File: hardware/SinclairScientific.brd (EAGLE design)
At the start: 50.8 x 22.9 mm, 33 parts, among them SW1 SPST_TACT-KMR2, U2 SPX3819-3.3, U3 MCP73831T-2ACI/OT, X1 JSTPH, X2 32.768, X3 microUSB

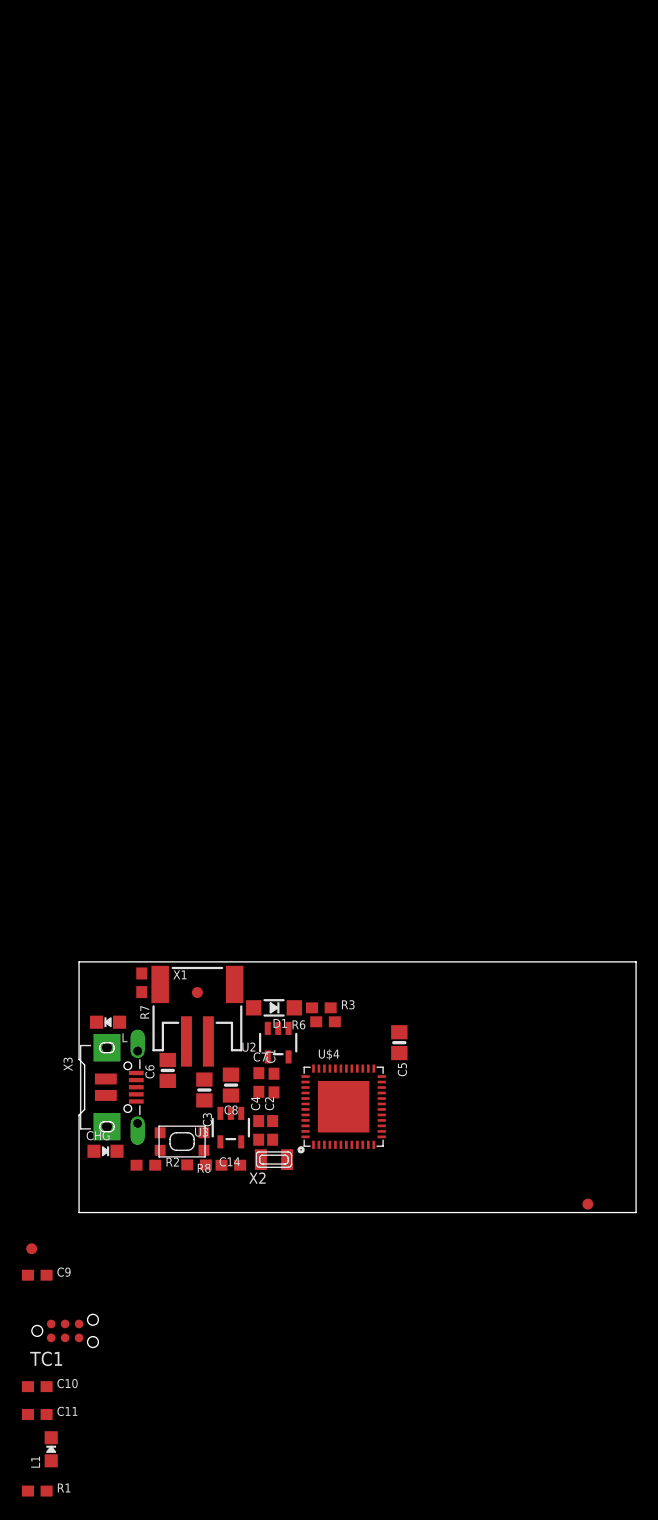
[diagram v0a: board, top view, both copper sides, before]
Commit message: Added more to schematic, started PCB placement, still WIP
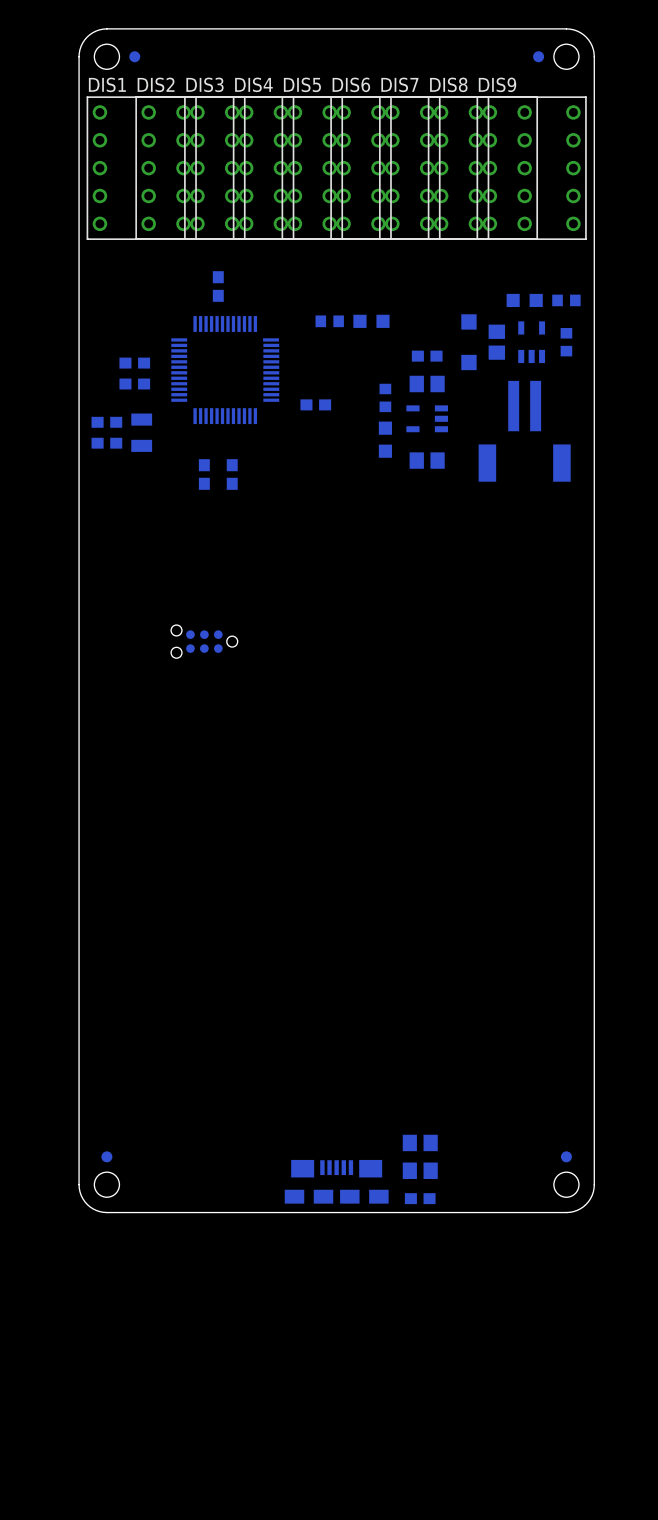
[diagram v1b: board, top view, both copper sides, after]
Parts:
- removed L: RED, SinclairScientific:CHIPLED_0805_NOOUTLINE
- removed R3: 100k, SinclairScientific:0603-NO
- removed R6: 100K, SinclairScientific:0603-NO
- removed SW1: SPST_TACT-KMR2, SinclairScientific:KMR2
- removed U$4: ATSAMD21G18_QFN, SinclairScientific:TQFN48_7MM
- removed X1: JSTPH, SinclairScientific:JSTPH2
- removed X3: microUSB, SinclairScientific:4UCONN_20329_V2
- added C12: 1uF, gametroller:C0603
- added C13: 10uF, gametroller:C0805
- added DIS1, DIS2, DIS3, DIS4, DIS5, DIS6, DIS7, DIS8, DIS9: LED_7-SEGMENT, SinclairScientific:HDSP-E
- added F1: 500mA, gametroller:R0805
- added J1: JSTPH, SinclairScientific:JSTPH2
- added J3: USB-MICRO, gametroller:USB-10118192-0001LF
- added L2: RED, SinclairScientific:CHIPLED_0805_NOOUTLINE
- added U$2: FIDUCIAL"", SinclairScientific:FIDUCIAL_1MM
- added U4: ATSAMD21G18, gametroller:TQFP48_7MM
- C1, C10, C11, C14, C2, C4, C7, C9: device SinclairScientific:0603-NO -> gametroller:C0603
- C3, C6, C8: value 10µF -> 10uF; device SinclairScientific:0805-NO -> gametroller:C0805
- C5: value 10uF -> 100nF; device SinclairScientific:0805-NO -> gametroller:C0603
- R1, R2, R7, R8: device SinclairScientific:0603-NO -> gametroller:R0603
- moved R1 104.6 mm to (27.9, 74.3), flipped to the bottom, turned to 270 degrees
- moved C10 101.7 mm to (12.7, 84.5), flipped to the bottom, turned to 90 degrees
- moved L1 97.0 mm to (27.9, 70.5), flipped to the bottom, turned to 180 degrees
- moved C11 95.5 mm to (21.6, 73.7), flipped to the bottom, turned to 180 degrees
- moved R2 87.7 mm to (44.5, 83.2), flipped to the bottom, turned to 180 degrees
- moved CHG 86.5 mm to (40.6, 83.2), flipped to the bottom, turned to 90 degrees
- moved U$34 85.5 mm to (5.08, 105.4), flipped to the bottom
- moved C9 83.7 mm to (5.08, 77.5), flipped to the bottom
- moved R8 81.1 mm to (44.5, 79.4), flipped to the bottom, turned to 270 degrees
- moved U3 76.7 mm to (41.3, 79.4), flipped to the bottom, turned to 0 degrees
- moved C3 73.2 mm to (38.1, 79.4), flipped to the bottom, turned to 90 degrees
- moved C14 71.4 mm to (5.08, 75.6), flipped to the bottom
- moved C7 68.0 mm to (31.8, 78.1), flipped to the bottom, turned to 180 degrees
- moved X2 67.4 mm to (5.71, 71.1), flipped to the bottom, turned to 270 degrees
- moved C8 66.4 mm to (31.8, 75.6), flipped to the bottom, turned to 180 degrees
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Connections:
- removed net D+: U$4.34, X3.D+
- removed net D-: U$4.33, X3.D-
- removed net GND1: L1.C
- new net LED_A: DIS1.10, DIS2.10, DIS3.10, DIS4.10, DIS5.10, DIS6.10, DIS7.10, DIS8.10, DIS9.10
- new net LED_B: DIS1.9, DIS2.9, DIS3.9, DIS4.9, DIS5.9, DIS6.9, DIS7.9, DIS8.9, DIS9.9
- new net LED_C: DIS1.7, DIS2.7, DIS3.7, DIS4.7, DIS5.7, DIS6.7, DIS7.7, DIS8.7, DIS9.7
- new net LED_CA1: DIS1.3, DIS1.8
- new net LED_CA2: DIS2.3, DIS2.8
- new net LED_CA3: DIS3.3, DIS3.8
- new net LED_CA4: DIS4.3, DIS4.8
- new net LED_CA5: DIS5.3, DIS5.8
- new net LED_CA6: DIS6.3, DIS6.8
- new net LED_CA7: DIS7.3, DIS7.8
- new net LED_CA8: DIS8.3, DIS8.8
- new net LED_CA9: DIS9.3, DIS9.8
- new net LED_D: DIS1.5, DIS2.5, DIS3.5, DIS4.5, DIS5.5, DIS6.5, DIS7.5, DIS8.5, DIS9.5
- new net LED_DP: DIS1.6, DIS2.6, DIS3.6, DIS4.6, DIS5.6, DIS6.6, DIS7.6, DIS8.6, DIS9.6
- new net LED_E: DIS1.4, DIS2.4, DIS3.4, DIS4.4, DIS5.4, DIS6.4, DIS7.4, DIS8.4, DIS9.4
- new net LED_F: DIS1.2, DIS2.2, DIS3.2, DIS4.2, DIS5.2, DIS6.2, DIS7.2, DIS8.2, DIS9.2
- new net LED_G: DIS1.1, DIS2.1, DIS3.1, DIS4.1, DIS5.1, DIS6.1, DIS7.1, DIS8.1, DIS9.1
- new net N$8: F1.1, J3.1
- new net RXD: U4.38
- new net RXLED: U4.48
- new net TXD: U4.37
- new net TXLED: U4.39
- new net USB_DM: J3.2, U4.33
- new net USB_DP: J3.3, U4.34
- net !RESET: now also TC1.1, U4.40; no longer SW1.1, SW1.3, U$4.40
- net +3V3: now also R1.1, TC1.2, U4.17, U4.36, U4.44, U4.6; no longer U$4.17, U$4.36, U$4.44, U$4.6
- net A0: now also U4.3; no longer U$4.3
- net A1: now also U4.7; no longer U$4.7
- net A2: now also U4.8; no longer U$4.8
- net A3: now also U4.9; no longer U$4.9
- net A4: now also U4.10; no longer U$4.10
- net A5: now also U4.47; no longer U$4.47
- net AREF: now also U4.4; no longer U$4.4
- net D0: now also U4.16; no longer U$4.16
- net D1: now also U4.15; no longer U$4.15
- net D10: now also U4.27; no longer U$4.27
- net D11: now also U4.25; no longer U$4.25
- net D12: now also U4.28; no longer U$4.28
- net D13: now also U4.26; no longer U$4.26
- net D2: now also U4.23; no longer U$4.23
- net D3: now also U4.14; no longer U$4.14
- net D4: now also U4.13; no longer U$4.13
- net D5: now also U4.24; no longer U$4.24
- net D6: now also U4.29; no longer U$4.29
- net D7: now also U4.30; no longer U$4.30
- net D8: now also U4.11; no longer U$4.11
- net D9: now also U4.12; no longer R3.2, R6.1, U$4.12
- net GND: now also C12.2, C13.2, J1.1, J3.5, L1.C, L2.C, TC1.3, U4.18, U4.35, U4.42, U4.5; no longer L.C, R6.2, SW1.2, SW1.4, U$4.18, U$4.35, U$4.42, U$4.5, U$4.THERMAL, X1.1, X3.BASE@1, X3.BASE@2, X3.GND, X3.SPRT@1, X3.SPRT@2, X3.SPRT@3, X3.SPRT@4
- net MISO: now also U4.21; no longer U$4.21
- net MOSI: now also U4.19; no longer U$4.19
- net N$2: now also L2.A; no longer L.A
- net N$5: now also U4.1; no longer U$4.1
- net N$7: now also U4.2; no longer U$4.2
- net SCK: now also U4.20; no longer U$4.20
- net SCL: now also U4.32; no longer U$4.32
- net SDA: now also U4.31; no longer U$4.31
- net SWCLK: now also TC1.5, U4.45; no longer U$4.45
- net SWDIO: now also TC1.4, U4.46; no longer U$4.46
- net VBAT: now also J1.2; no longer R3.1, X1.2
- net VBUS: now also C12.1, C13.1, F1.2; no longer X3.VBUS
- net VDDCORE: now also U4.43; no longer U$4.43
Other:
- board size 50.8 x 22.9 mm -> 47 x 108 mm

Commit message: Schematic nearly finalized, still working on board dimensions and component placement
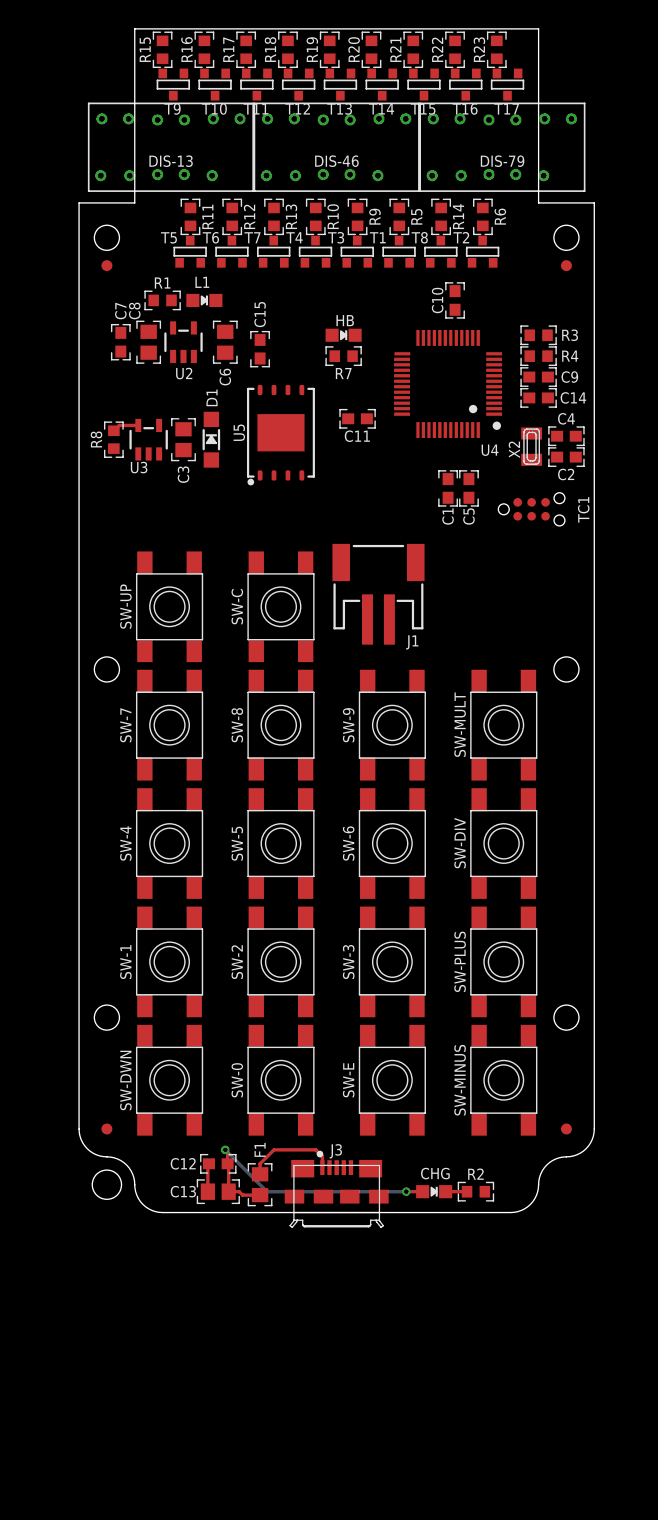
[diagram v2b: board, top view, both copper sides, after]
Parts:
- removed DIS1, DIS2, DIS3, DIS4, DIS5, DIS6, DIS7, DIS8, DIS9: LED_7-SEGMENT, SinclairScientific:HDSP-E
- removed L2: RED, SinclairScientific:CHIPLED_0805_NOOUTLINE
- added C15: 100nF, SinclairScientific:C0603
- added DIS-13, DIS-46, DIS-79: LED_3X7-SEGMENT, SinclairScientific:2352B
- added HB: RED, SinclairScientific:CHIPLED_0805_NOOUTLINE
- added R10, R11, R12, R13, R14, R5, R6, R9: 150, SinclairScientific:R0603
- added R15, R16, R17, R18, R19, R20, R21, R22, R23: 1k, SinclairScientific:R0603
- added R3, R4: 3.3k, SinclairScientific:R0603
- added SW-0, SW-1, SW-2, SW-3, SW-4, SW-5, SW-6, SW-7, SW-8, SW-9, SW-C, SW-DIV, SW-DWN, SW-E, SW-MINUS, SW-MULT, SW-PLUS, SW-UP: SPST_TACT-6X6, SinclairScientific:TACT_6X6
- added T1, T10, T11, T12, T13, T14, T15, T16, T17, T2, T3, T4, T5, T6, T7, T8, T9: (no value), SinclairScientific:SOT-23
- added U5: W25Q128JVSO, SinclairScientific:SON127P800X600X80-9N
- C1, C10, C11, C12, C14, C2, C4, C5, C7, C9: device gametroller:C0603 -> SinclairScientific:C0603
- C13, C3, C6, C8: device gametroller:C0805 -> SinclairScientific:C0805
- CHG: value ORANGE -> RED
- F1: device gametroller:R0805 -> SinclairScientific:R0805
- J3: device gametroller:USB-10118192-0001LF -> SinclairScientific:USB-10118192-0001LF
- R1, R2, R7, R8: device gametroller:R0603 -> SinclairScientific:R0603
- U4: device gametroller:TQFP48_7MM -> SinclairScientific:TQFP48_7MM
- moved CHG 81.7 mm to (32.4, 1.91), flipped to the top, turned to 270 degrees
- moved R2 81.7 mm to (36.2, 1.91), flipped to the top, turned to 0 degrees
- moved R8 42.2 mm to (3.17, 70.5), flipped to the top
- moved C2 41.9 mm to (44.5, 68.9), flipped to the top
- moved C4 41.9 mm to (44.5, 70.8), flipped to the top
- moved C14 36.9 mm to (41.9, 74.3), flipped to the top
- moved C9 36.9 mm to (41.9, 76.2), flipped to the top
- moved U3 36.0 mm to (6.35, 70.5), flipped to the top
- moved X2 35.6 mm to (41.3, 69.8), flipped to the top
- moved TC1 32.2 mm to (41.3, 64.1), flipped to the top
- moved C3 29.9 mm to (9.53, 70.5), flipped to the top
- moved C7 28.0 mm to (3.81, 79.4), flipped to the top, turned to 270 degrees
- moved C8 25.7 mm to (6.35, 79.4), flipped to the top, turned to 270 degrees
- moved D1 25.1 mm to (12.1, 70.5), flipped to the top
- moved U2 23.3 mm to (9.53, 79.4), flipped to the top, turned to 0 degrees
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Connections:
- net RXD renamed D31
- net RXLED renamed D25/RXLED
- net SCL renamed D21/SCL
- net SDA renamed D20/SDA
- net TXD renamed D30
- net TXLED renamed D26/TXLED
- removed net A0: U4.3
- removed net A1: U4.7
- removed net A2: U4.8
- removed net A3: U4.9
- removed net A4: U4.10
- removed net A5: U4.47
- removed net D8: U4.11
- removed net D9: U4.12
- removed net MISO: U4.21
- removed net MOSI: U4.19
- removed net SCK: U4.20
- new net D14/A0: T7.3, U4.3
- new net D15/A1: SW-2.B, SW-2.B', SW-DWN.B, SW-DWN.B', T15.3, U4.7
- new net D16/A2: SW-8.B, SW-8.B', SW-E.B, SW-E.B', T13.3, U4.8
- new net D17/A3: SW-7.B, SW-7.B', SW-UP.B, SW-UP.B', T12.3, U4.9
- new net D18/A4: T8.3, U4.10
- new net D19/A5: T4.3, U4.47
- new net D22/MISO: U4.21, U5.2
- new net D23/MOSI: U4.19, U5.5
- new net D24/SCK: U4.20, U5.6
- new net D27: U4.41
- new net D39: U4.22, U5.1
- new net D8/A6: R4.1, SW-0.A, SW-0.A', SW-C.A, SW-C.A', SW-DIV.A, SW-DIV.A', SW-DWN.A, SW-DWN.A', SW-E.A, SW-E.A', SW-MINUS.A, SW-MINUS.A', SW-MULT.A, SW-MULT.A', SW-PLUS.A, SW-PLUS.A', SW-UP.A, SW-UP.A', T2.3, U4.11
- new net D9/A7: R3.1, SW-1.A, SW-1.A', SW-2.A, SW-2.A', SW-3.A, SW-3.A', SW-4.A, SW-4.A', SW-5.A, SW-5.A', SW-6.A, SW-6.A', SW-7.A, SW-7.A', SW-8.A, SW-8.A', SW-9.A, SW-9.A', T5.3, U4.12
- new net N$10: R6.2, T2.1
- new net N$11: R9.2, T3.1
- new net N$12: R10.2, T4.1
- new net N$13: R11.2, T5.1
- new net N$14: R12.2, T6.1
- new net N$15: R13.2, T7.1
- new net N$16: R14.2, T8.1
- new net N$9: R5.2, T1.1
- net +3V3: now also C15.1, T10.1, T11.1, T12.1, T13.1, T14.1, T15.1, T16.1, T17.1, T9.1, U5.3, U5.7, U5.8
- net D10: now also T3.3
- net D11: now also SW-3.B, SW-3.B', SW-PLUS.B, SW-PLUS.B', T16.3
- net D12: now also SW-4.B, SW-4.B', SW-MINUS.B, SW-MINUS.B', T17.3
- net D2: now also SW-1.B, SW-1.B', SW-C.B, SW-C.B', T9.3
- net D3: now also SW-5.B, SW-5.B', SW-DIV.B, SW-DIV.B', T10.3
- net D4: now also SW-6.B, SW-6.B', SW-MULT.B, SW-MULT.B', T11.3
- net D5: now also T1.3
- net D6: now also T6.3
- net D7: now also SW-0.B, SW-0.B', SW-9.B, SW-9.B', T14.3
- net GND: now also C15.2, HB.C, R15.2, R16.2, R17.2, R18.2, R19.2, R20.2, R21.2, R22.2, R23.2, R3.2, R4.2, T1.2, T2.2, T3.2, T4.2, T5.2, T6.2, T7.2, T8.2, U5.4, U5.9; no longer L2.C
- net LED_A: now also DIS-13.11, DIS-46.11, DIS-79.11, R5.1; no longer DIS1.10, DIS2.10, DIS3.10, DIS4.10, DIS5.10, DIS6.10, DIS7.10, DIS8.10, DIS9.10
- net LED_B: now also DIS-13.7, DIS-46.7, DIS-79.7, R6.1; no longer DIS1.9, DIS2.9, DIS3.9, DIS4.9, DIS5.9, DIS6.9, DIS7.9, DIS8.9, DIS9.9
- net LED_C: now also DIS-13.4, DIS-46.4, DIS-79.4, R9.1; no longer DIS1.7, DIS2.7, DIS3.7, DIS4.7, DIS5.7, DIS6.7, DIS7.7, DIS8.7, DIS9.7
- net LED_CA1: now also DIS-13.12, R15.1, T9.2; no longer DIS1.3, DIS1.8
- net LED_CA2: now also DIS-13.9, R16.1, T10.2; no longer DIS2.3, DIS2.8
- net LED_CA3: now also DIS-13.8, R17.1, T11.2; no longer DIS3.3, DIS3.8
- net LED_CA4: now also DIS-46.12, R18.1, T12.2; no longer DIS4.3, DIS4.8
- net LED_CA5: now also DIS-46.9, R19.1, T13.2; no longer DIS5.3, DIS5.8
- net LED_CA6: now also DIS-46.8, R20.1, T14.2; no longer DIS6.3, DIS6.8
- net LED_CA7: now also DIS-79.12, R21.1, T15.2; no longer DIS7.3, DIS7.8
- net LED_CA8: now also DIS-79.9, R22.1, T16.2; no longer DIS8.3, DIS8.8
- net LED_CA9: now also DIS-79.8, R23.1, T17.2; no longer DIS9.3, DIS9.8
- net LED_D: now also DIS-13.2, DIS-46.2, DIS-79.2, R10.1; no longer DIS1.5, DIS2.5, DIS3.5, DIS4.5, DIS5.5, DIS6.5, DIS7.5, DIS8.5, DIS9.5
- net LED_DP: now also DIS-13.3, DIS-46.3, DIS-79.3, R14.1; no longer DIS1.6, DIS2.6, DIS3.6, DIS4.6, DIS5.6, DIS6.6, DIS7.6, DIS8.6, DIS9.6
- net LED_E: now also DIS-13.1, DIS-46.1, DIS-79.1, R11.1; no longer DIS1.4, DIS2.4, DIS3.4, DIS4.4, DIS5.4, DIS6.4, DIS7.4, DIS8.4, DIS9.4
- net LED_F: now also DIS-13.10, DIS-46.10, DIS-79.10, R12.1; no longer DIS1.2, DIS2.2, DIS3.2, DIS4.2, DIS5.2, DIS6.2, DIS7.2, DIS8.2, DIS9.2
- net LED_G: now also DIS-13.5, DIS-46.5, DIS-79.5, R13.1; no longer DIS1.1, DIS2.1, DIS3.1, DIS4.1, DIS5.1, DIS6.1, DIS7.1, DIS8.1, DIS9.1
- net N$2: now also HB.A; no longer L2.A
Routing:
- net VBUS: track 0.00 -> 26.5 mm, vias 0 -> 2
- net N$8: track 0.00 -> 8.43 mm
- net GND: track 0.00 -> 2.58 mm
- net N$4: track 0.00 -> 2.43 mm
- net N$1: track 0.00 -> 1.95 mm
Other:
- outline, holes or cut-outs redrawn
